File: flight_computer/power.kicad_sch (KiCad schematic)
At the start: 15 parts, among them J1 Conn_01x02, Q1 Q_NMOS_GSD, U3 TPS63051RMWR

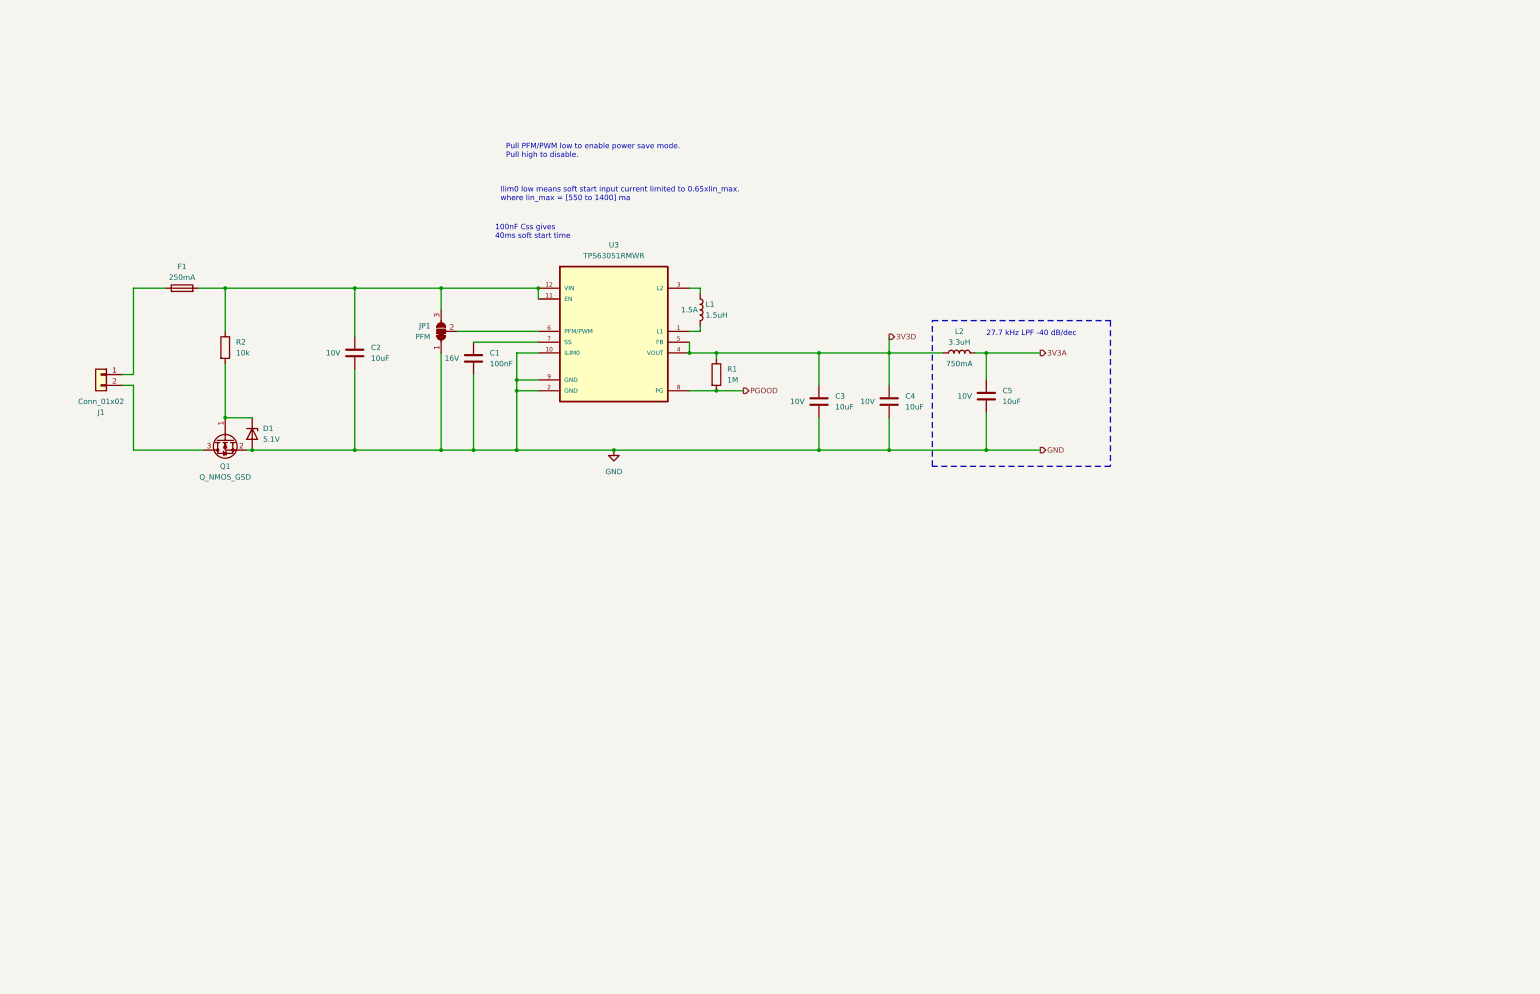
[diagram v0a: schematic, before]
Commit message: Adding current shunt measurement, amplification, filtering
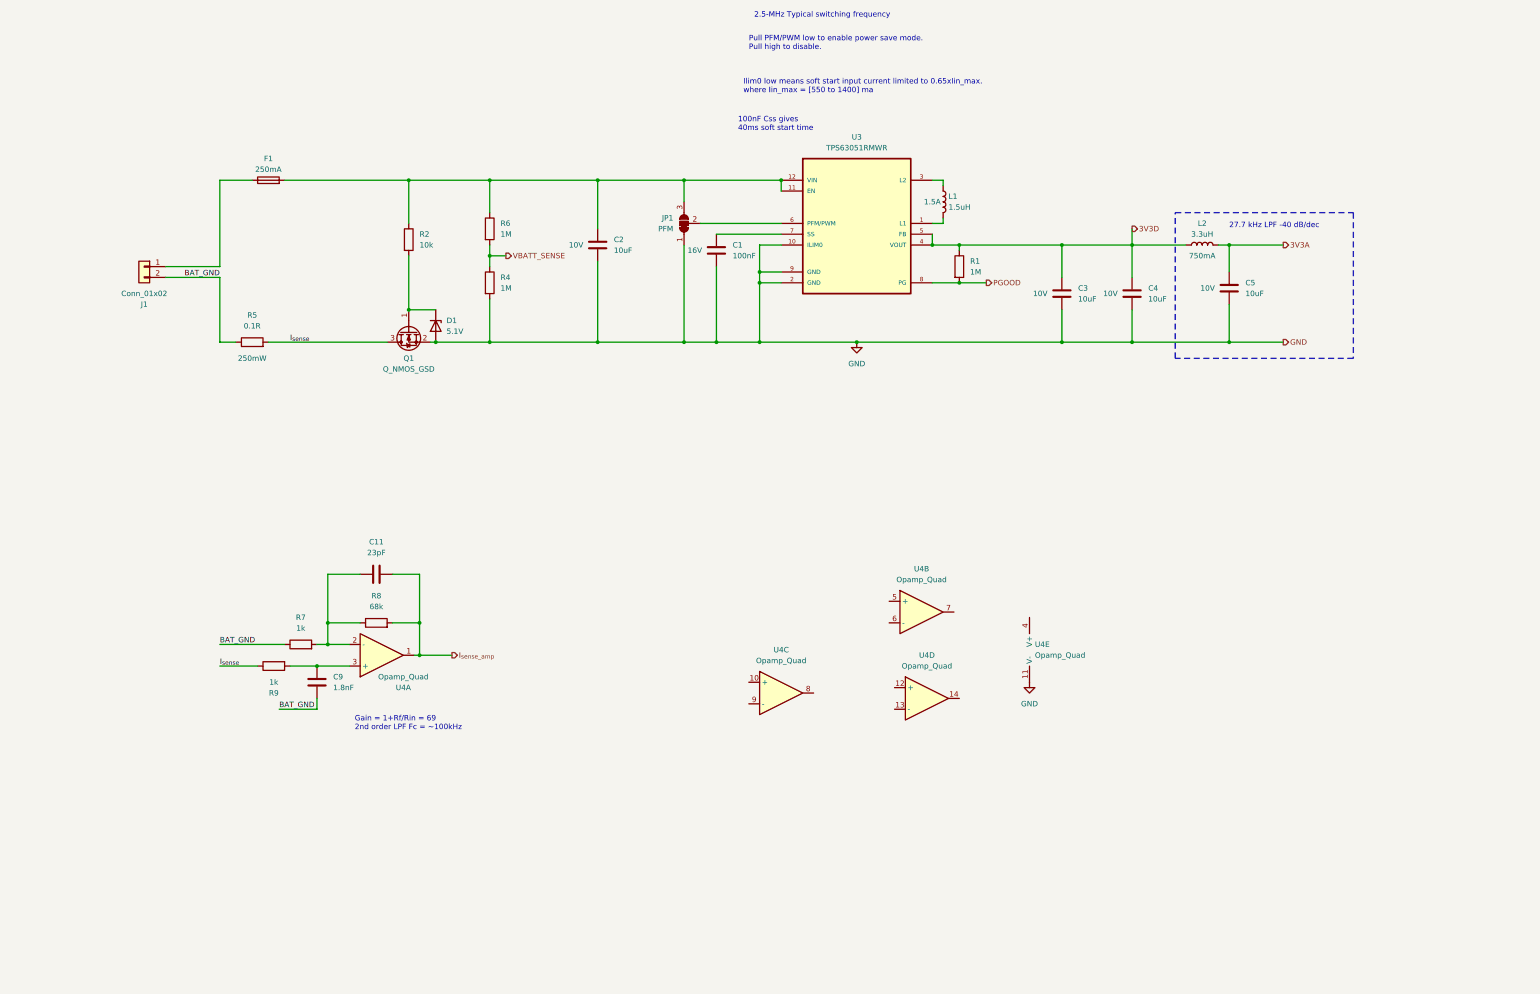
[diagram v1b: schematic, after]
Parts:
- added C11: 23pF, symbol Device:C
- added C9: 1.8nF, symbol Device:C
- added R4, R6: 1M, Resistor_SMD:R_0402_1005Metric, symbol Device:R
- added R5: 0.1R, Resistor_SMD:R_1206_3216Metric, symbol Device:R
- added R7, R9: 1k, symbol Device:R
- added R8: 68k, symbol Device:R
- added U4: Opamp_Quad, Package_SO:SOIC-14_3.9x8.7mm_P1.27mm, symbol Device:Opamp_Quad
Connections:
- net GND: now also R4.2, U4.11 (V-)
- net at C2.1, F1.2, JP1.3 (B)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: now also R6.1
- net BAT_GND: now reaches J1.2 (Pin_2)
- net BAT_GND: now also C9.2, R5.1, R7.1; no longer Q1.3 (D)
- new net: C9.1, R9.2, U4.3 (+)
- new net: C11.2, R7.2, R8.1, U4.2 (-)
- new net I_{sense_amp}: C11.1, R8.2, U4.1
- new net I_{sense}: Q1.3 (D), R5.2, R9.1
- new net VBATT_SENSE: R4.1, R6.2
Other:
- note added: "2.5-MHz Typical switching frequency"
- note added: "Gain = 1+Rf/Rin = 69 2nd order LPF Fc = ~100kHz"
- moved on the sheet: C1, C2, C3, C4, C5, D1, F1, J1, JP1, L1, L2, Q1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

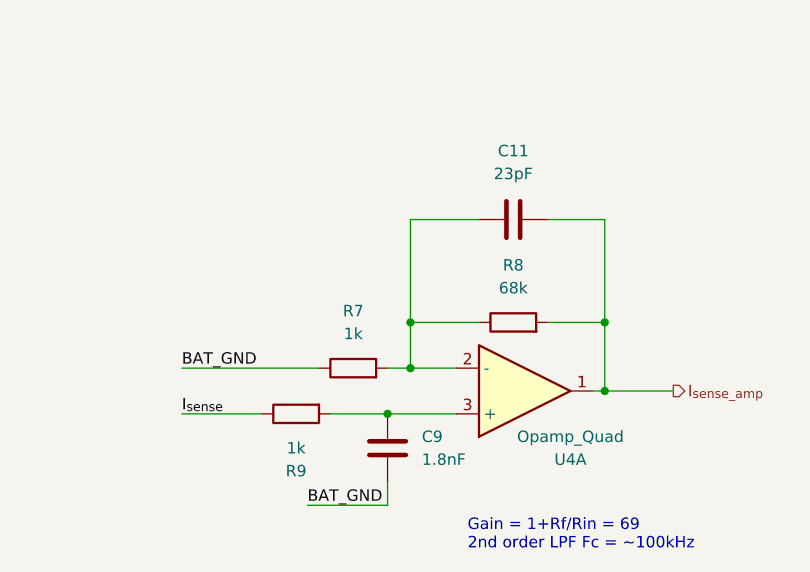
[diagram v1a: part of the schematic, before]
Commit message: Buzzer, LEDs, added actual components for current sensing and others I had missed
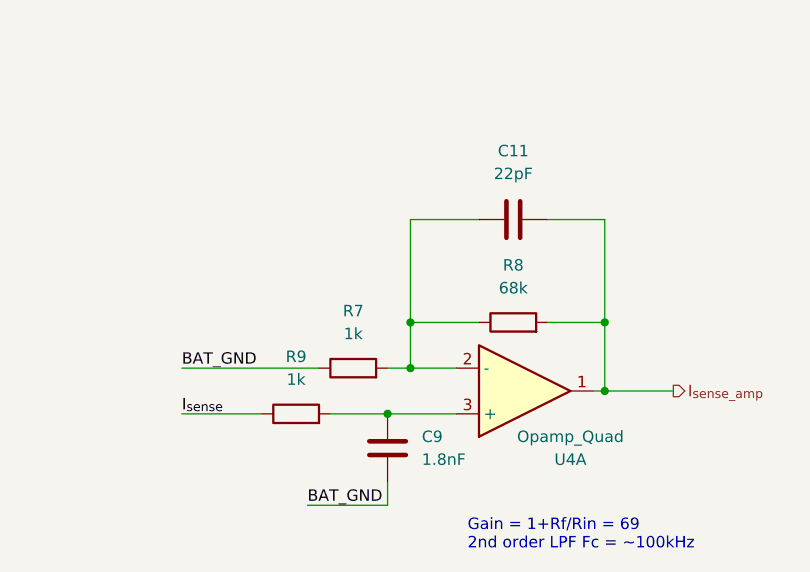
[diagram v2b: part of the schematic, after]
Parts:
- C11: value 23pF -> 22pF; footprint (none) -> Capacitor_SMD:C_0402_1005Metric; Manufacturer PN (none) -> 399-17554-1-ND; Supplier (none) -> Digikey; Supplier PN (none) -> C0402C220K4RAC7867
- C9: footprint (none) -> Capacitor_SMD:C_0402_1005Metric; Manufacturer PN (none) -> 399-17371-1-ND; Supplier (none) -> Digikey; Supplier PN (none) -> C0402C182K3RAC7867
- JP1: footprint (none) -> Jumper:SolderJumper-3_P1.3mm_Open_RoundedPad1.0x1.5mm_NumberLabels; now left out of the parts list
- Q1: footprint (none) -> Package_TO_SOT_SMD:SOT-323_SC-70; Manufacturer PN (none) -> PJC7404_R1_00001; Supplier (none) -> Digikey; Supplier PN (none) -> 3757-PJC7404_R1_00001CT-ND
- R7, R9: footprint (none) -> Resistor_SMD:R_0402_1005Metric; Manufacturer PN (none) -> 0402WGF1001TCE; Supplier (none) -> JLC; Supplier PN (none) -> C11702
- R8: footprint (none) -> Resistor_SMD:R_0402_1005Metric; Manufacturer PN (none) -> 0402WGF6802TCE; Supplier (none) -> JLC; Supplier PN (none) -> C36871
- U3: MPN TPS63051RMWR -> (none); Manufacturer PN (none) -> TPS63051RMWR; Supplier (none) -> Digikey; Supplier PN (none) -> 296-42650-1-ND

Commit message: PRessure sensor circuit
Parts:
- added C12: 100nF, Capacitor_SMD:C_0402_1005Metric, symbol Device:C
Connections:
- net 3V3D: now also U4.4 (V+), C12.1
- net GND: now also C12.2
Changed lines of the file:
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@@
   (junction (at 303.53 82.55) (diameter 0) (color 0 0 0 0)
   )
+  (junction (at 256.54 186.69) (diameter 0) (color 0 0 0 0)
+  )
   (junction (at 193.04 88.9) (diameter 0) (color 0 0 0 0)
   )
@@
   (junction (at 215.9 105.41) (diameter 0) (color 0 0 0 0)
   )
+  (wire (pts (xy 280.67 168.91) (xy 256.54 168.91))
+    (stroke (width 0) (type default))
+  )
   (wire (pts (xy 264.16 82.55) (xy 280.67 82.55))
     (stroke (width 0) (type default))
@@
     (stroke (width 0) (type default))
   )
+  (wire (pts (xy 256.54 187.96) (xy 256.54 186.69))
+    (stroke (width 0) (type default))
+  )
   (wire (pts (xy 240.03 91.44) (xy 246.38 91.44))
     (stroke (width 0) (type default))
@@
     (stroke (width 0) (type default))
   )
+  (wire (pts (xy 280.67 175.26) (xy 280.67 168.91))
+    (stroke (width 0) (type default))
+  )
   (wire (pts (xy 99.06 160.02) (xy 91.44 160.02))
     (stroke (width 0) (type default))
@@
     (stroke (width 0) (type default))
   )
+  (wire (pts (xy 280.67 182.88) (xy 280.67 186.69))
+    (stroke (width 0) (type default))
+  )
   (wire (pts (xy 236.22 76.2) (xy 236.22 77.47))
     (stroke (width 0) (type default))
@@
     (stroke (width 0) (type default))
   )
+  (wire (pts (xy 256.54 186.69) (xy 256.54 185.42))
+    (stroke (width 0) (type default))
+  )
   (wire (pts (xy 113.03 160.02) (xy 113.03 171.45))
     (stroke (width 0) (type default))
@@
     (stroke (width 0) (type default))
   )
+  (wire (pts (xy 256.54 168.91) (xy 256.54 170.18))
+    (stroke (width 0) (type default))
+  )
   (wire (pts (xy 193.04 91.44) (xy 198.12 91.44))
     (stroke (width 0) (type default))
   )
   (wire (pts (xy 182.88 105.41) (xy 193.04 105.41))
+    (stroke (width 0) (type default))
+  )
+  (wire (pts (xy 256.54 186.69) (xy 280.67 186.69))
     (stroke (width 0) (type default))
   )
@@
   )
   (label "I_{sense}" (at 82.55 105.41 0) (fields_autoplaced)
+    (effects (font (size 1.27 1.27)) (justify left bottom))
+  )
+  (label "3V3D" (at 270.51 82.55 0) (fields_autoplaced)
+    (effects (font (size 1.27 1.27)) (justify left bottom))
+  )
+  (label "3V3D" (at 265.43 168.91 0) (fields_autoplaced)
     (effects (font (size 1.27 1.27)) (justify left bottom))
   )
@@
     )
   )
+  (symbol (lib_id "Device:C") (at 280.67 179.07 0) (unit 1)
+    (in_bom yes) (on_board yes) (dnp no)
+    (property "Reference" "C12" (at 284.48 177.8 0)
+      (effects (font (size 1.27 1.27)) (justify left))
+    )
+    (property "Value" "100nF" (at 284.48 180.34 0)
+      (effects (font (size 1.27 1.27)) (justify left))
+    )
+    (property "Footprint" "Capacitor_SMD:C_0402_1005Metric" (at 281.6352 182.88 0)
+      (effects (font (size 1.27 1.27)) hide)
+    )
+    (property "Datasheet" "https://wmsc.lcsc.com/wmsc/upload/file/pdf/v2/lcsc/2304140030_Samsung-Electro-Mechanics-CL05B104KO5NNNC_C1525.pdf" (at 280.67 179.07 0)
+      (effects (font (size 1.27 1.27)) hide)
+    )
+    (property "Manufacturer PN" "CL05B104KO5NNNC" (at 280.67 179.07 0)
+      (effects (font (size 1.27 1.27)) hide)
+    )
+    (property "Supplier PN" "C1525" (at 280.67 179.07 0)
+      (effects (font (size 1.27 1.27)) hide)
+    )
+    (property "Supplier" "JLC" (at 280.67 179.07 0)
+      (effects (font (size 1.27 1.27)) hide)
+    )
+    (property "Voltage" "16V" (at 275.59 179.07 0)
+      (effects (font (size 1.27 1.27)))
+    )
+    (pin "1")
+    (pin "2")
+    (instances
+      (project "flight_computer"
+        (path "/89a81c02-14e9-456f-a334-ff69a24bd093/ebc948db-a9d3-410a-bdbf-1c31db890e56"
+          (reference "C12") (unit 1)
+        )
+      )
+    )
+  )
   (symbol (lib_id "Device:Opamp_Quad") (at 259.08 177.8 0) (unit 5)
     (in_bom yes) (on_board yes) (dnp no) (fields_autoplaced)
@@
     )
   )
-  (symbol (lib_id "power:GND") (at 256.54 185.42 0) (unit 1)
-    (in_bom yes) (on_board yes) (dnp no) (fields_autoplaced)
-    (property "Reference" "#PWR07" (at 256.54 191.77 0)
-      (effects (font (size 1.27 1.27)) hide)
-    )
-    (property "Value" "GND" (at 256.54 190.5 0)
-      (effects (font (size 1.27 1.27)))
-    )
-    (property "Footprint" "" (at 256.54 185.42 0)
-      (effects (font (size 1.27 1.27)) hide)
-    )
-    (property "Datasheet" "" (at 256.54 185.42 0)
-      (effects (font (size 1.27 1.27)) hide)
-    )
+  (symbol (lib_id "power:GND") (at 256.54 187.96 0) (unit 1)
+    (in_bom yes) (on_board yes) (dnp no) (fields_autoplaced)
+    (property "Reference" "#PWR07" (at 256.54 194.31 0)
+      (effects (font (size 1.27 1.27)) hide)
+    )
+    (property "Value" "GND" (at 256.54 193.04 0)
+      (effects (font (size 1.27 1.27)))
+    )
+    (property "Footprint" "" (at 256.54 187.96 0)
+      (effects (font (size 1.27 1.27)) hide)
+    )
+    (property "Datasheet" "" (at 256.54 187.96 0)
+      (effects (font (size 1.27 1.27)) hide)
+    )

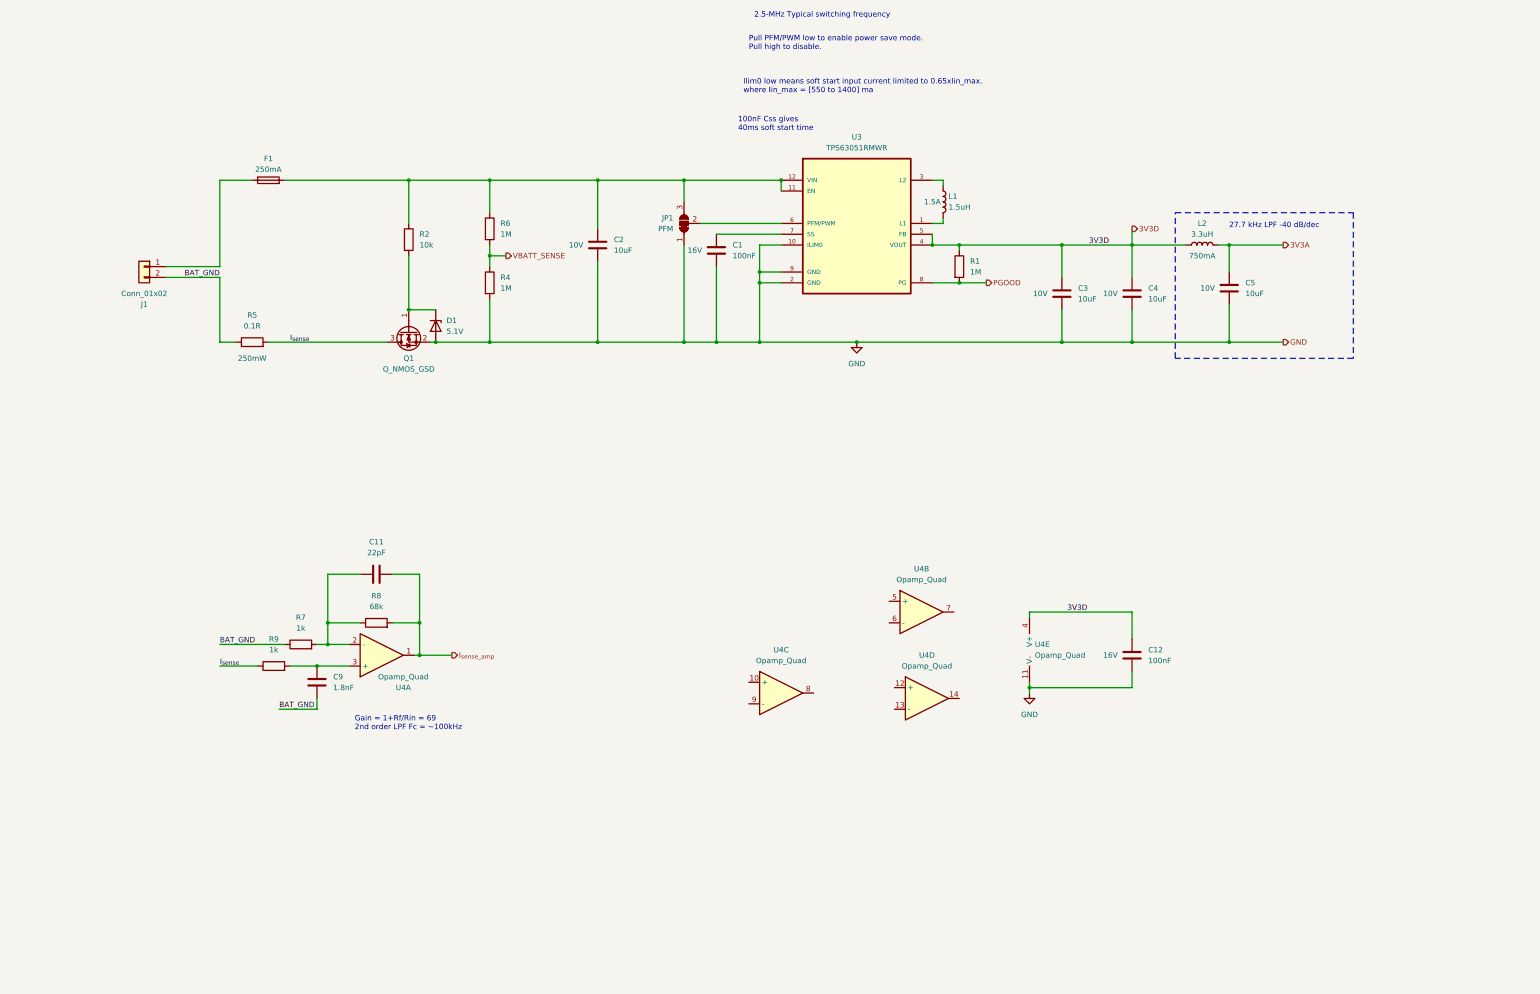
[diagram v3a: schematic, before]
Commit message: Tidying up schematics and adding most missing sections (Not finished GPS)
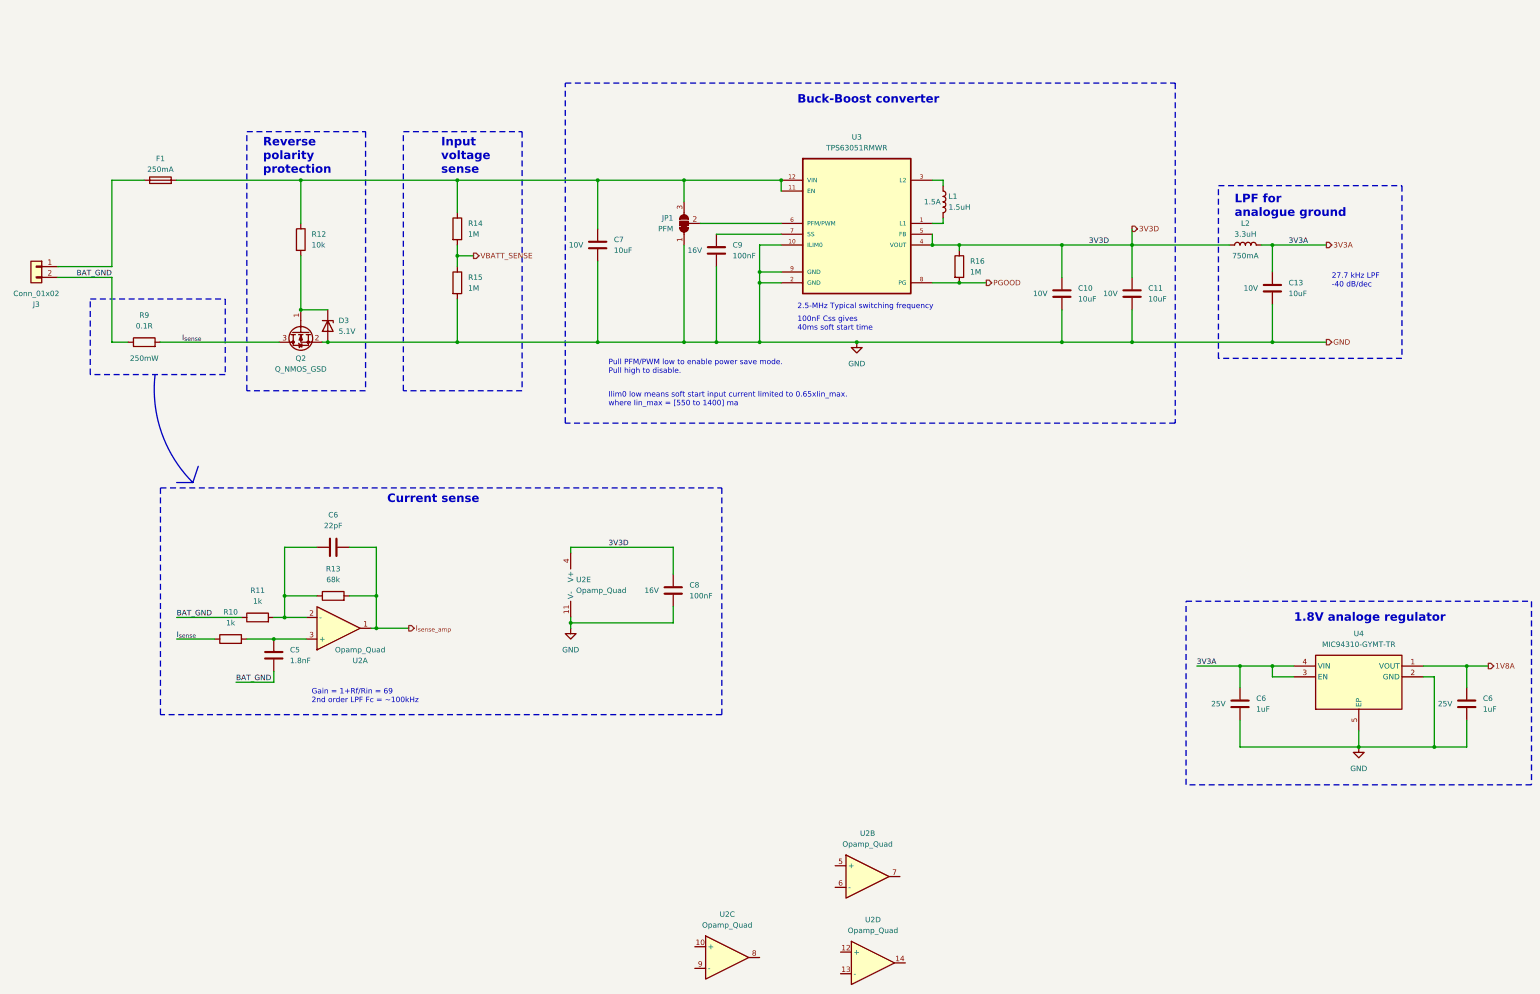
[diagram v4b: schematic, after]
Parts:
- added C6 (x2): 1uF, Capacitor_SMD:C_0402_1005Metric, symbol Device:C
- added U4: MIC94310-GYMT-TR, my_footprints:TDFN-4-1EP_1.2x1.6mm_P0.5mm, symbol my_library:MIC94310-GYMT-TR
- renumbered C3 to C10, C4 to C11, C5 to C13, C9 to C5, C11 to C6, C2 to C7, C12 to C8, C1 to C9, D1 to D3, J1 to J3, Q1 to Q2, R9 to R10, R7 to R11, R2 to R12, R8 to R13, R6 to R14, R4 to R15, R1 to R16, R5 to R9, U4 to U2
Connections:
- net 3V3A: now also C6.1, U4.3 (EN), U4.4 (VIN)
- net GND: now also C6.2, C6.2, U4.2 (GND), U4.5 (EP)
- new net 1V8A: C6.1, U4.1 (VOUT)
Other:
- note added: "1.8V analoge regulator"
- note added: "Buck-Boost converter"
- note added: "Current sense"
- note added: "Input voltage sense"
- note added: "LPF for analogue ground"
- note added: "Reverse polarity protection"
- moved on the sheet: C13, C5, C6, C8, D3, F1, J3, L2, Q2, R10, R11, R12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
